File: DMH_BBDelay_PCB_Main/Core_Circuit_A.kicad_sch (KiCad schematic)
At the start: 62 parts, among them Q3 J113, SW1 SW_DPDT_OnOffOn_x2, SW3 SW_SPDT, U1 TL074, U2 TL074, U3 V3205, U4 CD4046

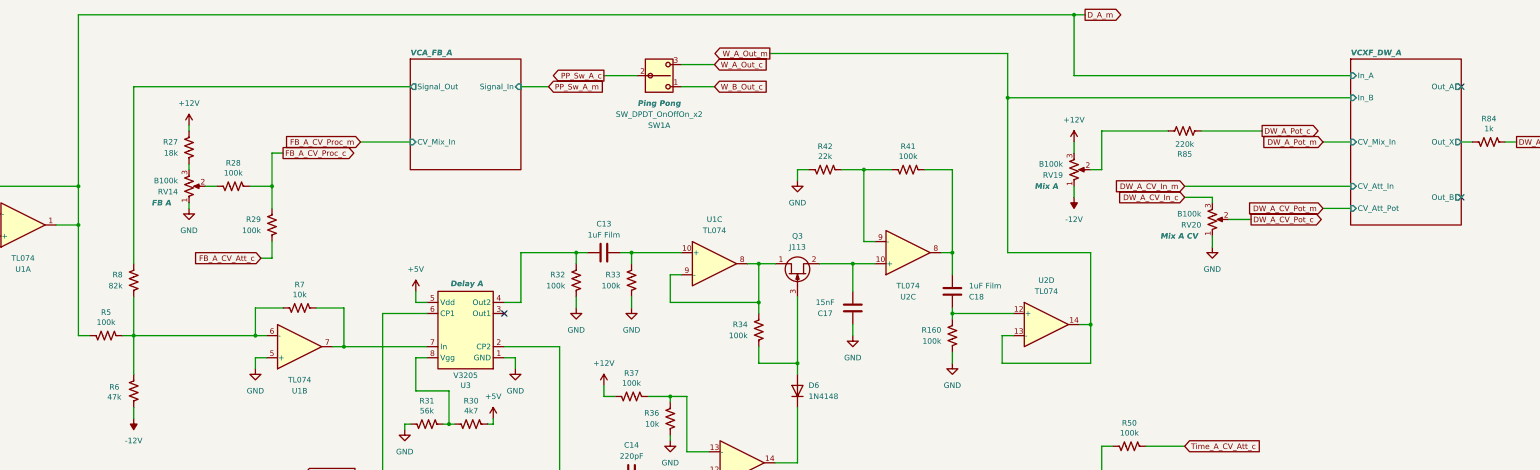
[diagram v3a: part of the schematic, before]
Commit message: Implemented tone control
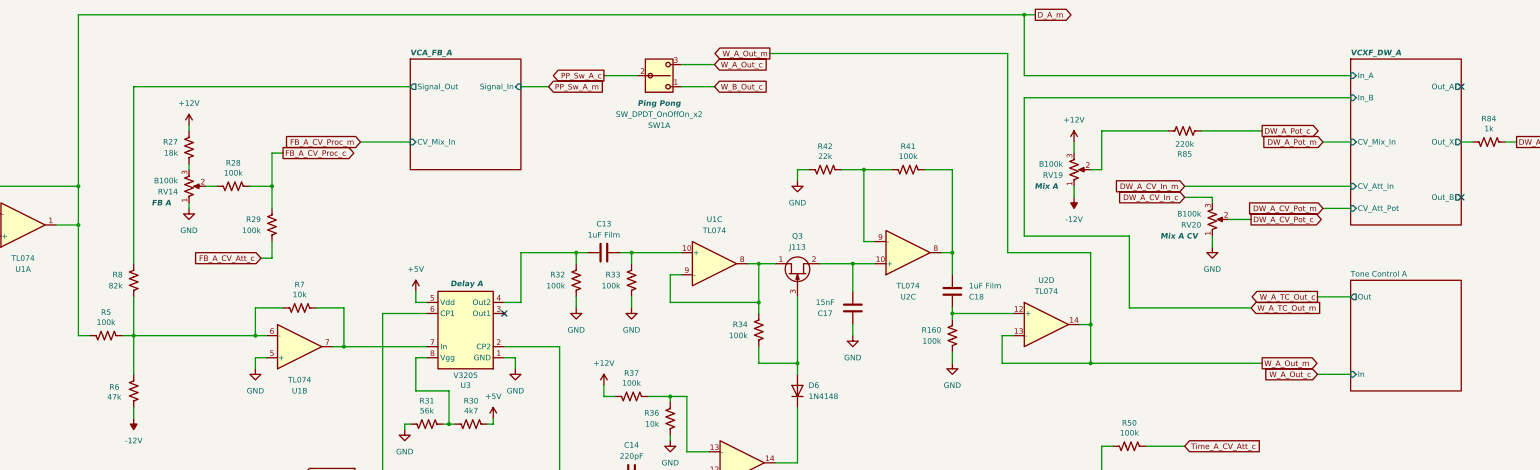
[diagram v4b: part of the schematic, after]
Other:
- added sheet Tone Control A (Tone_Control_A.kicad_sch)
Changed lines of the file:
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@@
 	)
 	(junction
+		(at 295.91 95.25)
+		(diameter 0)
+		(color 0 0 0 0)
+	)
+	(junction
 		(at 215.9 241.3)
 		(diameter 0)
@@
 	)
 	(junction
-		(at 276.86 34.29)
-		(diameter 0)
-		(color 0 0 0 0)
-	)
-	(junction
 		(at 270.51 147.32)
 		(diameter 0)
@@
 	)
 	(junction
-		(at 292.1 15.24)
+		(at 280.67 15.24)
 		(diameter 0)
 		(color 0 0 0 0)
@@
 	(wire
 		(pts
-			(xy 355.6 29.21) (xy 292.1 29.21)
+			(xy 355.6 29.21) (xy 280.67 29.21)
 		)
 		(stroke
@@
 	(wire
 		(pts
+			(xy 347.98 80.01) (xy 355.6 80.01)
+		)
+		(stroke
+			(width 0)
+			(type default)
+		)
+	)
+	(wire
+		(pts
+			(xy 280.67 66.04) (xy 280.67 34.29)
+		)
+		(stroke
+			(width 0)
+			(type default)
+		)
+	)
+	(wire
+		(pts
 			(xy 228.6 80.01) (xy 228.6 95.25)
 		)
@@
 	(wire
 		(pts
-			(xy 276.86 34.29) (xy 276.86 69.85)
+			(xy 276.86 24.13) (xy 276.86 69.85)
 		)
 		(stroke
@@
 	(wire
 		(pts
-			(xy 276.86 24.13) (xy 276.86 34.29)
-		)
-		(stroke
-			(width 0)
-			(type default)
-		)
-	)
-	(wire
-		(pts
 			(xy 137.16 165.1) (xy 137.16 171.45)
 		)
@@
 	(wire
 		(pts
-			(xy 292.1 29.21) (xy 292.1 15.24)
+			(xy 280.67 29.21) (xy 280.67 15.24)
 		)
 		(stroke
@@
 	(wire
 		(pts
+			(xy 304.8 82.55) (xy 332.74 82.55)
+		)
+		(stroke
+			(width 0)
+			(type default)
+		)
+	)
+	(wire
+		(pts
 			(xy 133.35 173.99) (xy 133.35 160.02)
 		)
@@
 	(wire
 		(pts
+			(xy 304.8 82.55) (xy 304.8 66.04)
+		)
+		(stroke
+			(width 0)
+			(type default)
+		)
+	)
+	(wire
+		(pts
 			(xy 133.35 120.65) (xy 133.35 142.24)
 		)
@@
 	(wire
 		(pts
+			(xy 304.8 66.04) (xy 280.67 66.04)
+		)
+		(stroke
+			(width 0)
+			(type default)
+		)
+	)
+	(wire
+		(pts
 			(xy 238.76 50.8) (xy 243.84 50.8)
 		)
@@
 	(wire
 		(pts
+			(xy 280.67 34.29) (xy 355.6 34.29)
+		)
+		(stroke
+			(width 0)
+			(type default)
+		)
+	)
+	(wire
+		(pts
 			(xy 308.61 114.3) (xy 317.5 114.3)
 		)
@@
 	(wire
 		(pts
-			(xy 276.86 34.29) (xy 355.6 34.29)
-		)
-		(stroke
-			(width 0)
-			(type default)
-		)
-	)
-	(wire
-		(pts
 			(xy 232.41 127) (xy 241.3 127)
 		)
@@
 	(wire
 		(pts
+			(xy 295.91 95.25) (xy 335.28 95.25)
+		)
+		(stroke
+			(width 0)
+			(type default)
+		)
+	)
+	(wire
+		(pts
 			(xy 63.5 181.61) (xy 63.5 184.15)
 		)
@@
 	(wire
 		(pts
-			(xy 292.1 15.24) (xy 63.5 15.24)
+			(xy 280.67 15.24) (xy 63.5 15.24)
 		)
 		(stroke
@@
 	(wire
 		(pts
+			(xy 347.98 97.79) (xy 355.6 97.79)
+		)
+		(stroke
+			(width 0)
+			(type default)
+		)
+	)
+	(wire
+		(pts
 			(xy 105.41 71.12) (xy 107.95 71.12)
 		)
@@
 	(wire
 		(pts
-			(xy 292.1 15.24) (xy 294.64 15.24)
+			(xy 280.67 15.24) (xy 283.21 15.24)
 		)
 		(stroke
@@
 	(global_label "D_A_m"
 		(shape output)
-		(at 294.64 15.24 0)
+		(at 283.21 15.24 0)
 		(fields_autoplaced yes)
 		(effects
@@
 		)
 		(property "Intersheetrefs" "${INTERSHEET_REFS}"
-			(at 303.6123 15.24 0)
+			(at 292.1823 15.24 0)
 			(hide yes)
 			(show_name no)
@@
 		)
 	)
+	(global_label "W_A_TC_Out_c"
+		(shape output)
+		(at 347.98 80.01 180)
+		(fields_autoplaced yes)
+		(effects
+			(font
+				(size 1.27 1.27)
+			)
+			(justify right)
+		)
+		(property "Intersheetrefs" "${INTERSHEET_REFS}"
+			(at 332.053 80.01 0)
+			(hide yes)
+			(show_name no)
+			(do_not_autoplace no)
+			(effects
+				(font
+					(size 1.27 1.27)
+				)
+				(justify right)
+			)
+		)
+	)
+	(global_label "W_A_Out_c"
+		(shape input)
+		(at 347.98 97.79 180)
+		(fields_autoplaced yes)
+		(effects
+			(font
+				(size 1.27 1.27)
+			)
+			(justify right)
+		)
+		(property "Intersheetrefs" "${INTERSHEET_REFS}"
+			(at 335.2582 97.79 0)
+			(hide yes)
+			(show_name no)
+			(do_not_autoplace no)
+			(effects
+				(font
+					(size 1.27 1.27)
+				)
+				(justify right)
+			)
+		)
+	)
 	(global_label "A_In_m"
 		(shape input)
@@
 		)
 	)
+	(global_label "W_A_Out_m"
+		(shape output)
+		(at 335.28 95.25 0)
+		(fields_autoplaced yes)
+		(effects
+			(font
+				(size 1.27 1.27)
+			)
+			(justify left)
+		)
+		(property "Intersheetrefs" "${INTERSHEET_REFS}"
+			(at 348.6065 95.25 0)
+			(hide yes)
+			(show_name no)
+			(do_not_autoplace no)
+			(effects
+				(font
+					(size 1.27 1.27)
+				)
+				(justify left)
+			)
+		)
+	)
 	(global_label "W_A_Out_c"
 		(shape input)
@@
 		)
 	)
+	(global_label "W_A_TC_Out_m"
+		(shape input)
+		(at 332.74 82.55 0)
+		(fields_autoplaced yes)
+		(effects
+			(font
+				(size 1.27 1.27)
+			)
+			(justify left)
+		)
+		(property "Intersheetrefs" "${INTERSHEET_REFS}"
+			(at 349.2717 82.55 0)
+			(hide yes)
+			(show_name no)
+			(do_not_autoplace no)
+			(effects
+				(font
+					(size 1.27 1.27)
+				)
+				(justify left)
+			)
+		)
+	)
 	(global_label "Time_A_CV_Proc_m"
 		(shape input)
@@
 			(project "DMH_BBDelay_PCB_Main"
 				(path "/58f4306d-5387-4983-bb08-41a2313fd315/7ad2d702-dfb7-4d49-a82d-34430dd5948f"
-					(page "7")
+					(page "6")
 				)
 			)
@@
 				)
 			)
+		)
+	)
+	(sheet
+		(at 355.6 76.2)
+		(size 25.4 25.4)
+		(exclude_from_sim no)
+		(in_bom yes)
+		(on_board yes)
+		(dnp no)
+		(fields_autoplaced yes)
+		(stroke
+			(width 0.1524)
+			(type solid)
+		)
+		(fill
+			(color 0 0 0 0)
+		)
+		(property "Sheetname" "Tone Control A"
+			(at 355.6 75.4884 0)
+			(show_name no)
+			(do_not_autoplace no)
+			(effects
+				(font
+					(size 1.27 1.27)
+				)
+				(justify left bottom)
+			)
+		)
+		(property "Sheetfile" "Tone_Control_A.kicad_sch"
+			(at 355.6 102.1846 0)
+			(hide yes)
+			(show_name no)
+			(do_not_autoplace no)
+			(effects
+				(font
+					(size 1.27 1.27)
+				)
+				(justify left top)
+			)
+		)
+		(pin "In" input
+			(at 355.6 97.79 180)
+			(effects
+				(font
+					(size 1.27 1.27)
+				)
+				(justify left)
+			)
+		)
+		(pin "Out" output
+			(at 355.6 80.01 180)
+			(effects
+				(font
+					(size 1.27 1.27)
+				)
+				(justify left)
+			)
+		)
+		(instances
+			(project "DMH_BBDelay_PCB_Main"
+				(path "/58f4306d-5387-4983-bb08-41a2313fd315/7ad2d702-dfb7-4d49-a82d-34430dd5948f"
+					(page "10")
+				)
+			)

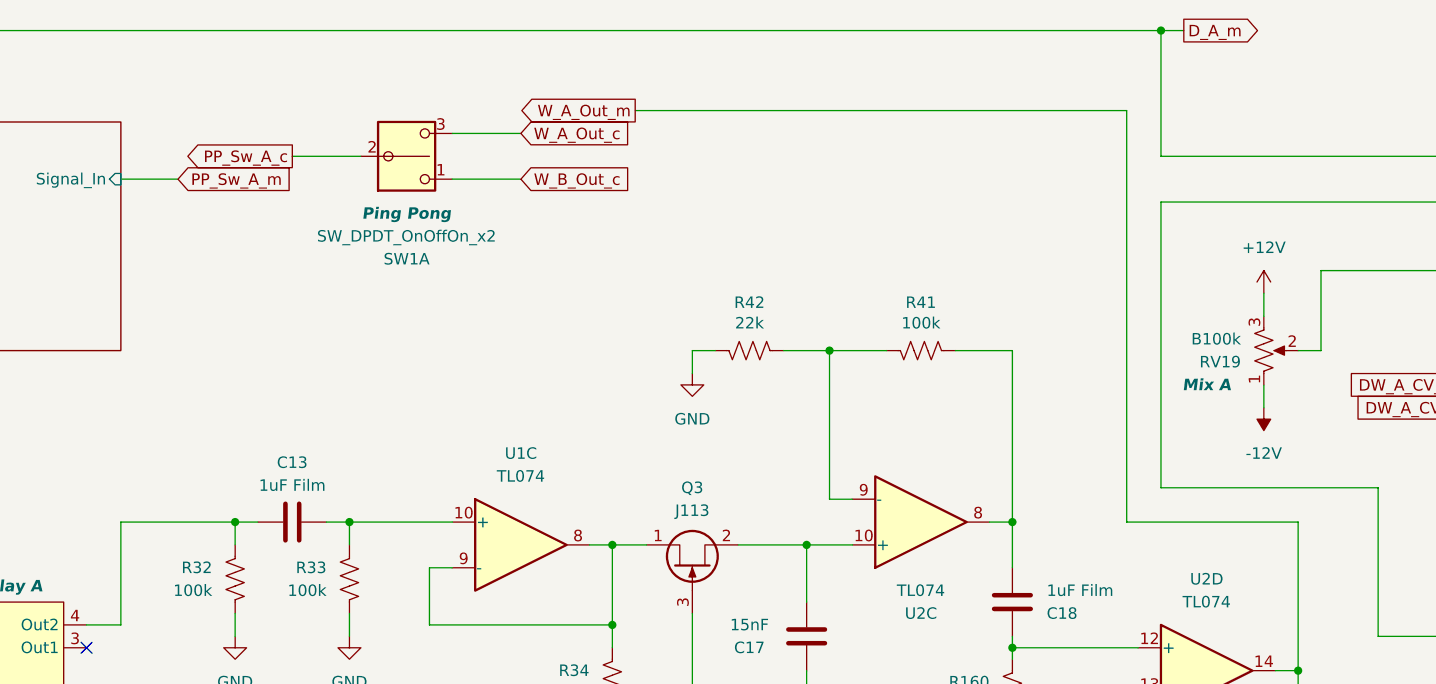
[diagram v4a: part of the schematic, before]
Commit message: Re-implemented Ping Pong mode with CD4053
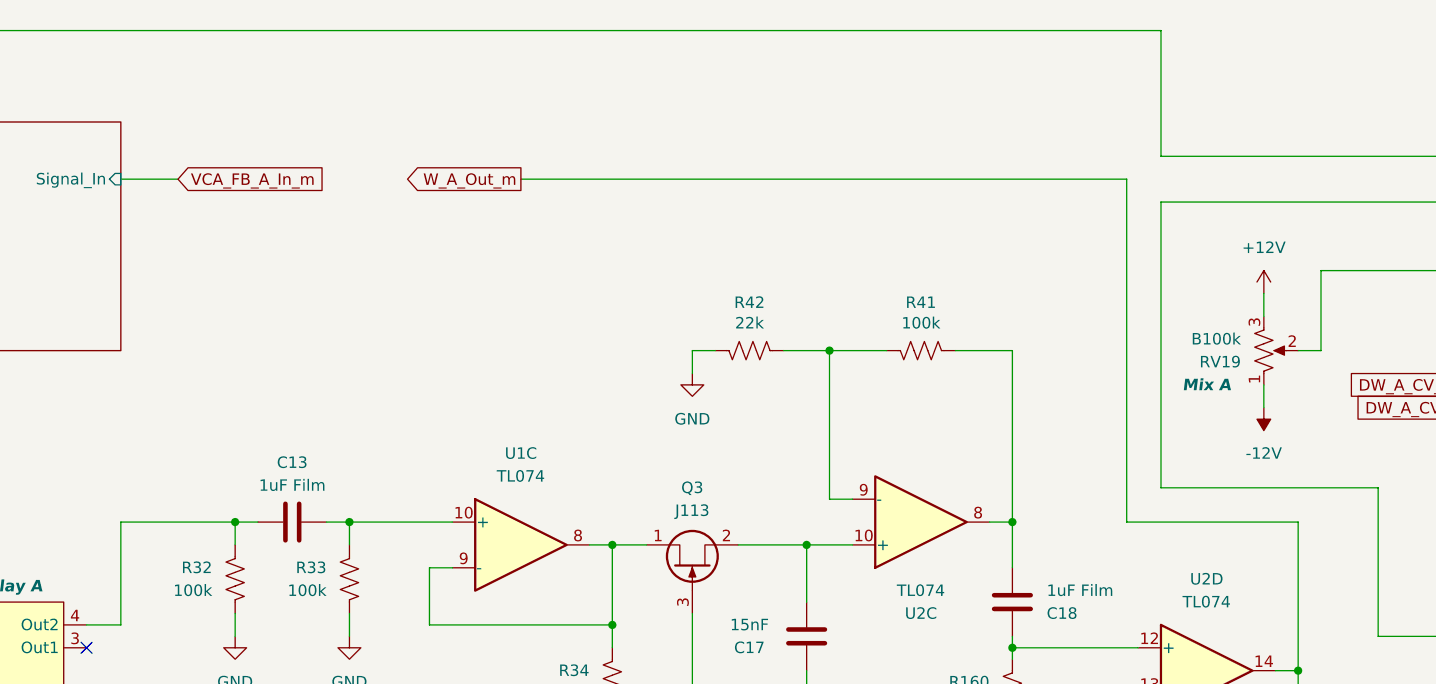
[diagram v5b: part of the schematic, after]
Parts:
- removed SW1: SW_DPDT_OnOffOn_x2, SynthStuff:Toggle_Switch_2_Poles_TE, symbol SynthStuff:SW_DPDT_OnOffOn_x2
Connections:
- net D_A_m renamed VCXF_DW_A/In_A

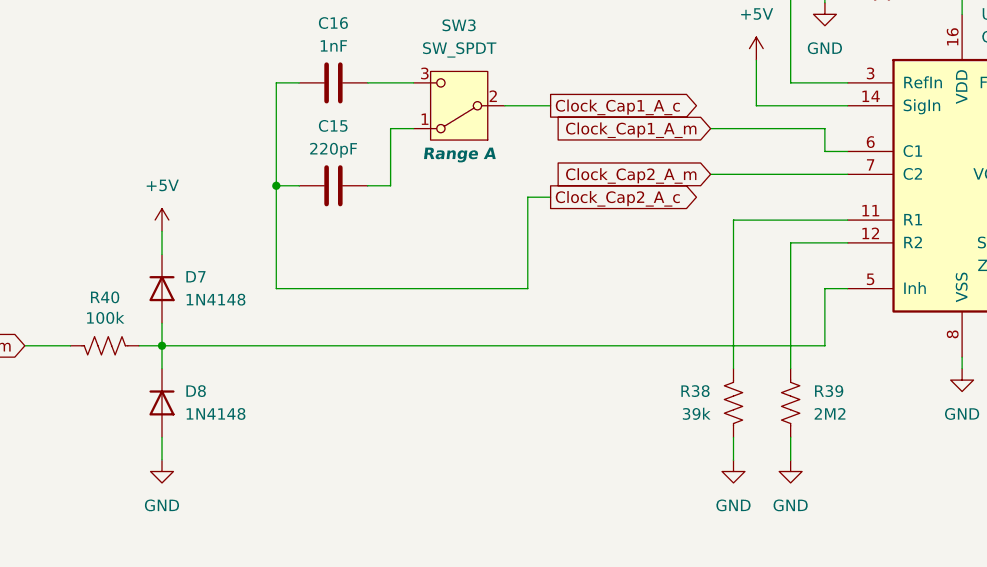
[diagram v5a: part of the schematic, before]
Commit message: Added schmit triggers to inhibt CV input paths
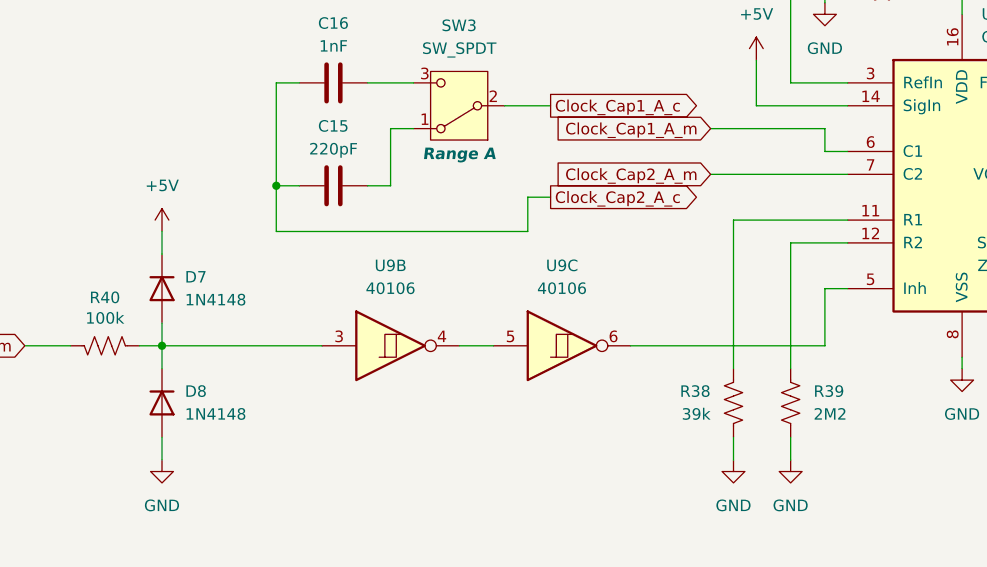
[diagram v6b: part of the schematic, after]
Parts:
- added U9: 40106, Package_DIP:DIP-14_W7.62mm_Socket, symbol 4xxx:40106
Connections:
- net at D7.2 (A), D8.1 (K), R40.2: now also U9.3; no longer U4.5 (Inh)
- new net: U9.4, U9.5
- new net: U4.5 (Inh), U9.6
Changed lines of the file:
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@@
 	)
 	(junction
-		(at 76.2 153.67)
+		(at 63.5 171.45)
 		(diameter 0)
 		(color 0 0 0 0)
 	)
 	(junction
-		(at 63.5 171.45)
+		(at 228.6 95.25)
 		(diameter 0)
 		(color 0 0 0 0)
 	)
 	(junction
-		(at 228.6 95.25)
+		(at 76.2 153.67)
 		(diameter 0)
 		(color 0 0 0 0)
@@
 	(wire
 		(pts
-			(xy 104.14 165.1) (xy 76.2 165.1)
+			(xy 104.14 158.75) (xy 76.2 158.75)
 		)
 		(stroke
@@
 	(wire
 		(pts
-			(xy 76.2 165.1) (xy 76.2 153.67)
+			(xy 76.2 158.75) (xy 76.2 153.67)
 		)
 		(stroke
@@
 	(wire
 		(pts
+			(xy 100.33 171.45) (xy 96.52 171.45)
+		)
+		(stroke
+			(width 0)
+			(type default)
+		)
+	)
+	(wire
+		(pts
 			(xy 241.3 72.39) (xy 246.38 72.39)
 		)
@@
 	(wire
 		(pts
-			(xy 104.14 154.94) (xy 104.14 165.1)
+			(xy 104.14 154.94) (xy 104.14 158.75)
 		)
 		(stroke
@@
 	(wire
 		(pts
+			(xy 81.28 171.45) (xy 63.5 171.45)
+		)
+		(stroke
+			(width 0)
+			(type default)
+		)
+	)
+	(wire
+		(pts
 			(xy 304.8 82.55) (xy 304.8 66.04)
 		)
@@
 	(wire
 		(pts
-			(xy 137.16 171.45) (xy 63.5 171.45)
+			(xy 137.16 171.45) (xy 115.57 171.45)
 		)
 		(stroke
@@
 	)
 	(symbol
+		(lib_id "4xxx:40106")
+		(at 88.9 171.45 0)
+		(unit 2)
+		(body_style 1)
+		(exclude_from_sim no)
+		(in_bom yes)
+		(on_board yes)
+		(in_pos_files yes)
+		(dnp no)
+		(fields_autoplaced yes)
+		(property "Reference" "U9"
+			(at 88.9 162.56 0)
+			(show_name no)
+			(do_not_autoplace no)
+			(effects
+				(font
+					(size 1.27 1.27)
+				)
+			)
+		)
+		(property "Value" "40106"
+			(at 88.9 165.1 0)
+			(show_name no)
+			(do_not_autoplace no)
+			(effects
+				(font
+					(size 1.27 1.27)
+				)
+			)
+		)
+		(property "Footprint" "Package_DIP:DIP-14_W7.62mm_Socket"
+			(at 88.9 171.45 0)
+			(hide yes)
+			(show_name no)
+			(do_not_autoplace no)
+			(effects
+				(font
+					(size 1.27 1.27)
+				)
+			)
+		)
+		(property "Datasheet" "https://assets.nexperia.com/documents/data-sheet/HEF40106B.pdf"
+			(at 88.9 171.45 0)
+			(hide yes)
+			(show_name no)
+			(do_not_autoplace no)
+			(effects
+				(font
+					(size 1.27 1.27)
+				)
+			)
+		)
+		(property "Description" "Hex Schmitt trigger inverter"
+			(at 88.9 171.45 0)
+			(hide yes)
+			(show_name no)
+			(do_not_autoplace no)
+			(effects
+				(font
+					(size 1.27 1.27)
+				)
+			)
+		)
+		(pin "3"
+		)
+		(pin "11"
+		)
+		(pin "9"
+		)
+		(pin "12"
+		)
+		(pin "2"
+		)
+		(pin "6"
+		)
+		(pin "13"
+		)
+		(pin "14"
+		)
+		(pin "4"
+		)
+		(pin "8"
+		)
+		(pin "1"
+		)
+		(pin "5"
+		)
+		(pin "10"
+		)
+		(pin "7"
+		)
+		(instances
+			(project "DMH_BBDelay_PCB_Main"
+				(path "/58f4306d-5387-4983-bb08-41a2313fd315/7ad2d702-dfb7-4d49-a82d-34430dd5948f"
+					(reference "U9")
+					(unit 2)
+				)
+			)
+		)
+	)
+	(symbol
 		(lib_id "Device:R_US")
 		(at 199.39 107.95 0)
@@
 				)
 			)
+		)
+	)
+	(symbol
+		(lib_id "4xxx:40106")
+		(at 107.95 171.45 0)
+		(unit 3)
+		(body_style 1)
+		(exclude_from_sim no)
+		(in_bom yes)
+		(on_board yes)
+		(in_pos_files yes)
+		(dnp no)
+		(fields_autoplaced yes)
+		(property "Reference" "U9"
+			(at 107.95 162.56 0)
+			(show_name no)
+			(do_not_autoplace no)
+			(effects
+				(font
+					(size 1.27 1.27)
+				)
+			)
+		)
+		(property "Value" "40106"
+			(at 107.95 165.1 0)
+			(show_name no)
+			(do_not_autoplace no)
+			(effects
+				(font
+					(size 1.27 1.27)
+				)
+			)
+		)
+		(property "Footprint" "Package_DIP:DIP-14_W7.62mm_Socket"
+			(at 107.95 171.45 0)
+			(hide yes)
+			(show_name no)
+			(do_not_autoplace no)
+			(effects
+				(font
+					(size 1.27 1.27)
+				)
+			)
+		)
+		(property "Datasheet" "https://assets.nexperia.com/documents/data-sheet/HEF40106B.pdf"
+			(at 107.95 171.45 0)
+			(hide yes)
+			(show_name no)
+			(do_not_autoplace no)
+			(effects
+				(font
+					(size 1.27 1.27)
+				)
+			)
+		)
+		(property "Description" "Hex Schmitt trigger inverter"
+			(at 107.95 171.45 0)
+			(hide yes)
+			(show_name no)
+			(do_not_autoplace no)
+			(effects
+				(font
+					(size 1.27 1.27)
+				)
+			)
+		)
+		(pin "3"
+		)
+		(pin "11"
+		)
+		(pin "9"
+		)
+		(pin "12"
+		)
+		(pin "2"
+		)
+		(pin "6"
+		)
+		(pin "13"
+		)
+		(pin "14"
+		)
+		(pin "4"
+		)
+		(pin "8"
+		)
+		(pin "1"
+		)
+		(pin "5"
+		)
+		(pin "10"
+		)
+		(pin "7"
+		)
+		(instances
+			(project "DMH_BBDelay_PCB_Main"
+				(path "/58f4306d-5387-4983-bb08-41a2313fd315/7ad2d702-dfb7-4d49-a82d-34430dd5948f"
+					(reference "U9")
+					(unit 3)
+				)
+			)
